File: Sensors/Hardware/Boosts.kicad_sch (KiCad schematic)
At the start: 17 parts

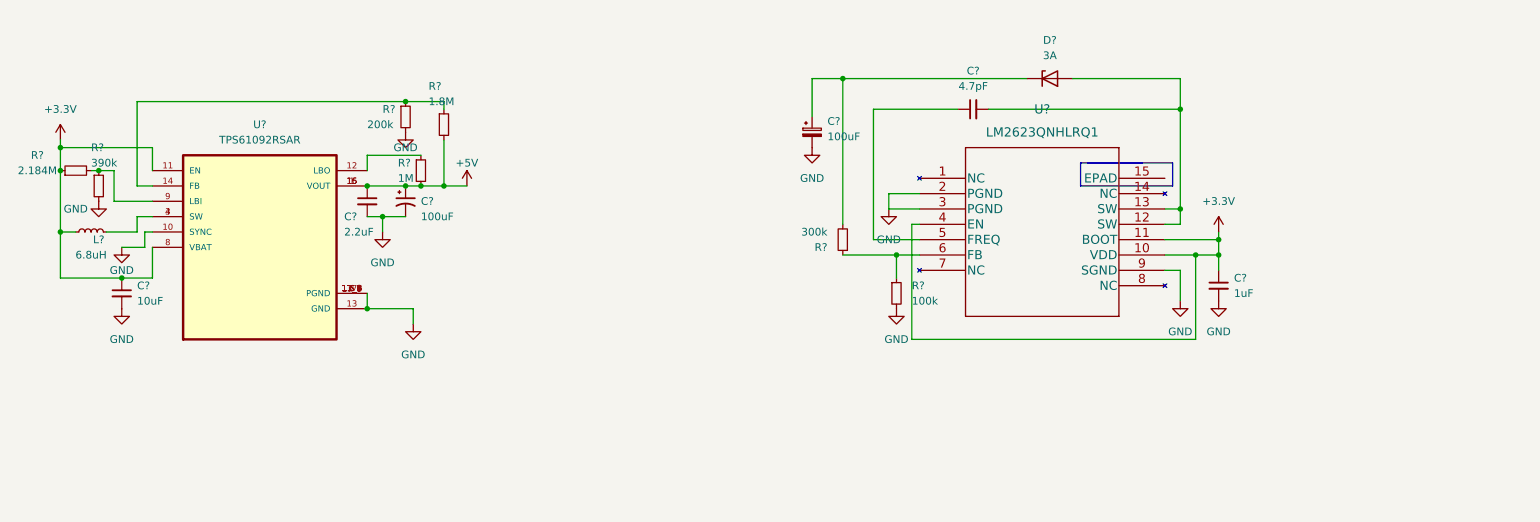
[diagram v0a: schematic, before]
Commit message: update
still need to fix 10v rail
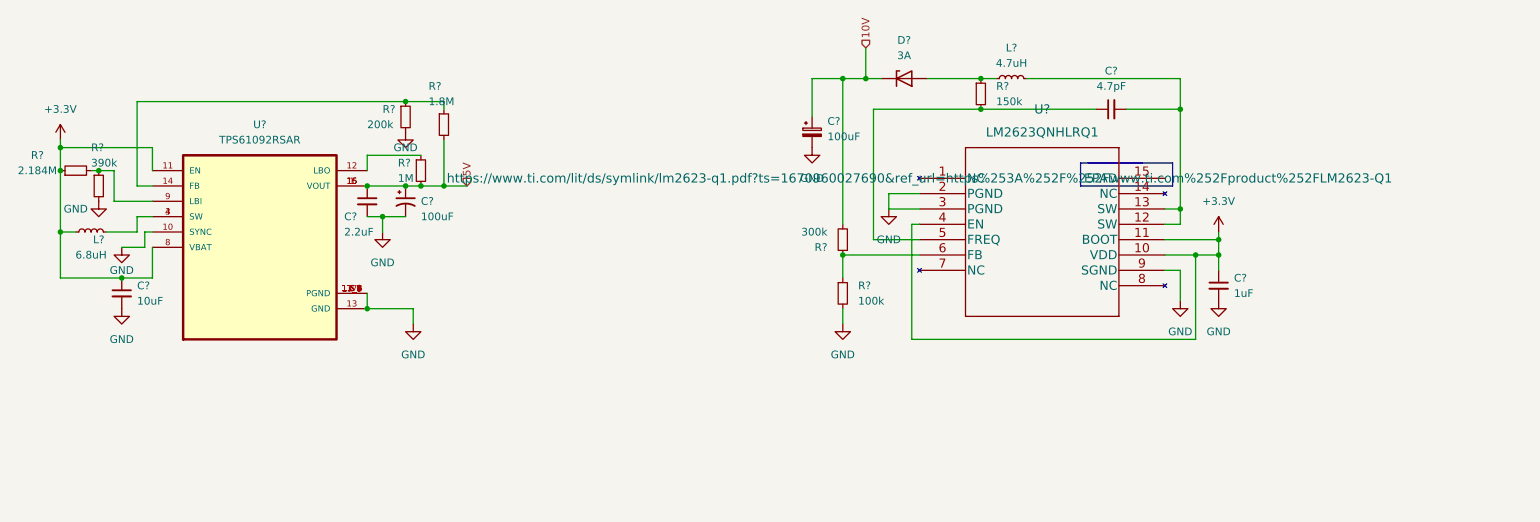
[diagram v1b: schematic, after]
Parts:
- added L?: 4.7uH, symbol Device:L_Small
- added R?: 150k, symbol Device:R_Small
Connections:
- net at C?.2, U?.12 (SW), U?.13 (SW): now also L?.2; no longer D?.2 (A)
- net at C?.1, U?.5 (FREQ): now also R?.2
- net 10V: now reaches C?.1, D?.1 (K), R?.2
- net +5V renamed 5V
- new net: D?.2 (A), L?.1, R?.1
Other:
- moved on the sheet: C?, D?, R?

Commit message: update 10v rail
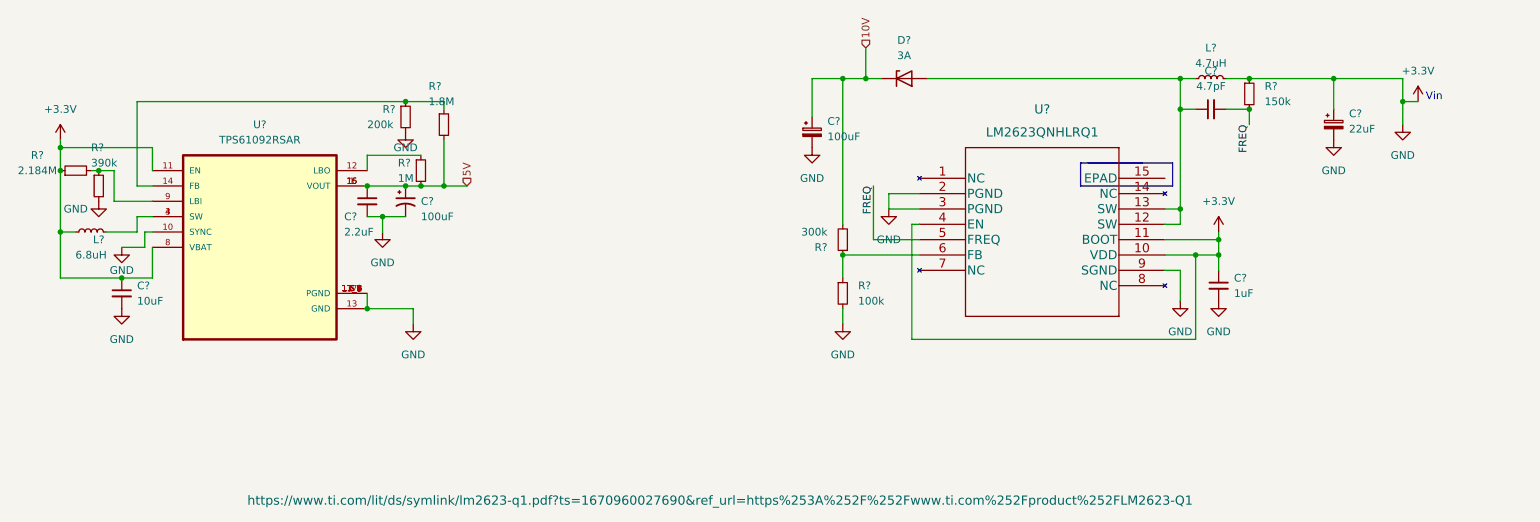
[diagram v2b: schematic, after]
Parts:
- added C?: 22uF, symbol Device:C_Polarized_Small
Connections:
- net GND is gone; now on net +3V3: C?.2, C?.2, C?.2, C?.2, C?.2, R?.2, R?.2, R?.2, U?.10 (SYNC), U?.13 (GND), U?.17 (PGND), U?.17_1 (PGND), U?.17_2 (PGND), U?.17_3 (PGND), U?.17_4 (PGND), U?.17_5 (PGND), U?.17_6 (PGND), U?.17_7 (PGND), U?.17_8 (PGND), U?.17_9 (PGND), U?.2 (PGND), U?.3 (PGND), U?.5 (PGND), U?.6 (PGND), U?.7 (PGND), U?.9 (SGND)
- net +3V3: now also L?.2, R?.1, C?.1, C?.2
- net at U?.12 (SW), U?.13 (SW): now also C?.1, D?.2 (A), L?.1; no longer C?.2, L?.2
- net FREQ: now reaches R?.2, U?.5 (FREQ)
- net FREQ: now also C?.2; no longer C?.1
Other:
- note added: "Vin"
- moved on the sheet: C?, L?, R?

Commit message: fp assignments
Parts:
- C51, C52: renamed from C?; footprint Capacitor_SMD:C_0603_1608Metric -> Capacitor_SMD:C_0402_1005Metric
- C53: renamed from C?; footprint iclr:CAPC2012X145N -> Capacitor_SMD:C_0603_1608Metric
- C54, C57: renamed from C?; footprint (none) -> Capacitor_SMD:C_0603_1608Metric
- C55, C56: renamed from C?; footprint (none) -> Capacitor_SMD:C_0402_1005Metric
- D1: renamed from D?; footprint (none) -> Diode_SMD:D_0603_1608Metric
- R59, R60: renamed from R?; footprint Resistor_SMD:R_0603_1608Metric -> Resistor_SMD:R_0402_1005Metric
- R63, R64, R65: renamed from R?; footprint (none) -> Resistor_SMD:R_0402_1005Metric
- gave numbers to parts that had none: 7
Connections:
- no-connect marks 0 -> 1

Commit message: grouping layout
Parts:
- L5: footprint (none) -> Inductor_SMD:L_0603_1608Metric
- U12: footprint NHL14_TEX -> iclr:LM2623QNHLRQ1
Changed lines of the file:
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@@
       (effects (font (size 1.524 1.524)))
     )
-    (property "Footprint" "NHL14_TEX" (id 2) (at 212.09 65.024 0)
+    (property "Footprint" "iclr:LM2623QNHLRQ1" (id 2) (at 212.09 65.024 0)
       (effects (font (size 1.524 1.524)) hide)
     )
@@
     (property "Reference" "L5" (id 0) (at 240.03 49.53 90))
     (property "Value" "4.7uH" (id 1) (at 240.03 52.07 90))
-    (property "Footprint" "" (id 2) (at 240.03 54.61 0)
-      (effects (font (size 1.27 1.27)) hide)
-    )
+    (property "Footprint" "Inductor_SMD:L_0603_1608Metric" (id 2) (at 240.03 54.61 0)
+      (effects (font (size 1.27 1.27)) hide)
+    )

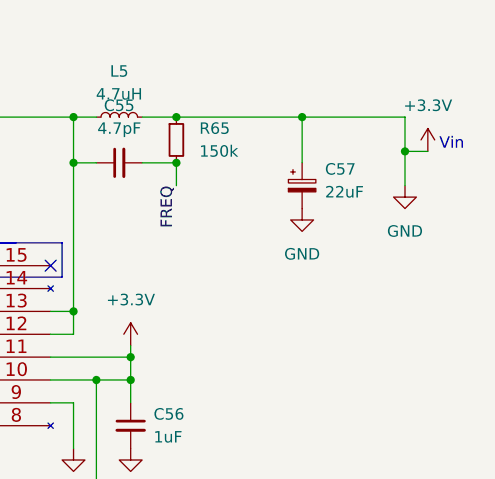
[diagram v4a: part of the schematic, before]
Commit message: nanofit placements
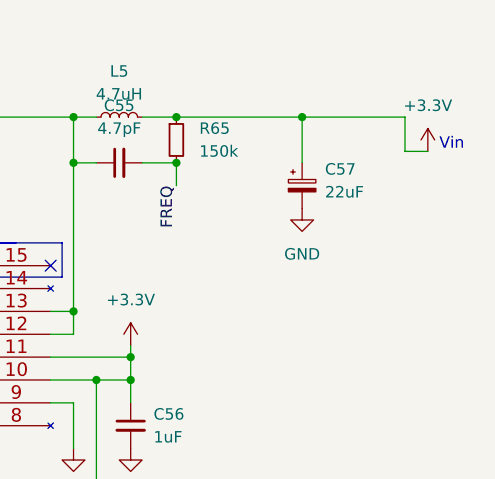
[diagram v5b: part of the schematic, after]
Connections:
- net +3V3: no longer C51.2, C52.2, C53.2, C54.2, C56.2, C57.2, R59.2, R60.2, R64.2, U11.10 (SYNC), U11.13 (GND), U11.17 (PGND), U11.17_1 (PGND), U11.17_2 (PGND), U11.17_3 (PGND), U11.17_4 (PGND), U11.17_5 (PGND), U11.17_6 (PGND), U11.17_7 (PGND), U11.17_8 (PGND), U11.17_9 (PGND), U11.5 (PGND), U11.6 (PGND), U11.7 (PGND), U12.2 (PGND), U12.3 (PGND), U12.9 (SGND)
- new net GND: C51.2, C52.2, C53.2, C54.2, C56.2, C57.2, R59.2, R60.2, R64.2, U11.10 (SYNC), U11.13 (GND), U11.17 (PGND), U11.17_1 (PGND), U11.17_2 (PGND), U11.17_3 (PGND), U11.17_4 (PGND), U11.17_5 (PGND), U11.17_6 (PGND), U11.17_7 (PGND), U11.17_8 (PGND), U11.17_9 (PGND), U11.5 (PGND), U11.6 (PGND), U11.7 (PGND), U12.2 (PGND), U12.3 (PGND), U12.9 (SGND)
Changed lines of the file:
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@@
   (junction (at 234.95 59.69) (diameter 0) (color 0 0 0 0)
-  )
-  (junction (at 271.78 58.42) (diameter 0) (color 0 0 0 0)
   )
   (junction (at 246.38 54.61) (diameter 0) (color 0 0 0 0)
@@
     (stroke (width 0) (type default) (color 0 0 0 0))
   )
-  (wire (pts (xy 271.78 58.42) (xy 271.78 62.23))
-    (stroke (width 0) (type default) (color 0 0 0 0))
-  )
   (wire (pts (xy 182.88 54.61) (xy 185.42 54.61))
     (stroke (width 0) (type default) (color 0 0 0 0))
@@
     (effects (font (size 1.27 1.27)) (justify left))
   )
-  (symbol (lib_id "power:GND") (at 271.78 62.23 0) (unit 1)
-    (in_bom yes) (on_board yes) (fields_autoplaced)
-    (property "Reference" "#PWR0144" (id 0) (at 271.78 68.58 0)
-      (effects (font (size 1.27 1.27)) hide)
-    )
-    (property "Value" "GND" (id 1) (at 271.78 67.31 0))
-    (property "Footprint" "" (id 2) (at 271.78 62.23 0)
-      (effects (font (size 1.27 1.27)) hide)
-    )
-    (property "Datasheet" "" (id 3) (at 271.78 62.23 0)
-      (effects (font (size 1.27 1.27)) hide)
-    )
-    (pin "1")
-  )
   (symbol (lib_id "power:GND") (at 106.68 63.5 0) (unit 1)

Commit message: update (tps and filters)
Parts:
- C53: footprint Capacitor_SMD:C_0603_1608Metric -> iclr:CAPC2012X145N
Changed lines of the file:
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@@
       (effects (font (size 1.27 1.27)) (justify left))
     )
-    (property "Footprint" "Capacitor_SMD:C_0603_1608Metric" (id 2) (at 106.68 74.93 0)
+    (property "Footprint" "iclr:CAPC2012X145N" (id 2) (at 106.68 74.93 0)
       (effects (font (size 1.27 1.27)) hide)
     )

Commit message: redimensioning to 120x50mm
also finished tps
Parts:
- C51, C52: footprint Capacitor_SMD:C_0402_1005Metric -> Capacitor_SMD:C_0603_1608Metric
- R59, R60: footprint Resistor_SMD:R_0402_1005Metric -> Resistor_SMD:R_0603_1608Metric
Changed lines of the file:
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@@
       (effects (font (size 1.27 1.27)) (justify left))
     )
-    (property "Footprint" "Resistor_SMD:R_0402_1005Metric" (id 2) (at 106.68 60.96 0)
+    (property "Footprint" "Resistor_SMD:R_0603_1608Metric" (id 2) (at 106.68 60.96 0)
       (effects (font (size 1.27 1.27)) hide)
     )
@@
       (effects (font (size 1.27 1.27)) (justify left))
     )
-    (property "Footprint" "Resistor_SMD:R_0402_1005Metric" (id 2) (at 55.88 72.39 0)
+    (property "Footprint" "Resistor_SMD:R_0603_1608Metric" (id 2) (at 55.88 72.39 0)
       (effects (font (size 1.27 1.27)) hide)
     )
@@
       (effects (font (size 1.27 1.27)) (justify left))
     )
-    (property "Footprint" "Capacitor_SMD:C_0402_1005Metric" (id 2) (at 59.69 90.17 0)
+    (property "Footprint" "Capacitor_SMD:C_0603_1608Metric" (id 2) (at 59.69 90.17 0)
       (effects (font (size 1.27 1.27)) hide)
     )
@@
       (effects (font (size 1.27 1.27)) (justify left))
     )
-    (property "Footprint" "Capacitor_SMD:C_0402_1005Metric" (id 2) (at 100.33 74.93 0)
-      (effects (font (size 1.27 1.27)) hide)
-    )
+    (property "Footprint" "Capacitor_SMD:C_0603_1608Metric" (id 2) (at 100.33 74.93 0)
+      (effects (font (size 1.27 1.27)) hide)
+    )
